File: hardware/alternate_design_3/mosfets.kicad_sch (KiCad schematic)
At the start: 3 parts, among them J2 Screw_Terminal_01x02, J3 Screw_Terminal_01x02, U5 ADUM3223ARZ

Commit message: updated alternate design
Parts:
- removed J2, J3: Screw_Terminal_01x02, symbol Connector:Screw_Terminal_01x02
- removed U5: ADUM3223ARZ, ADUM3223ARZ:SOIC127P600X175-16N, symbol ADUM3223ARZ:ADUM3223ARZ
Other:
- added sheet Gate Drive (gate_drive.kicad_sch)
- added sheet MCU (MCU.kicad_sch)
- added sheet OCP_Current_Sens (ocp_cur_sens.kicad_sch)
- added sheet Power Management (power_mgmt.kicad_sch)

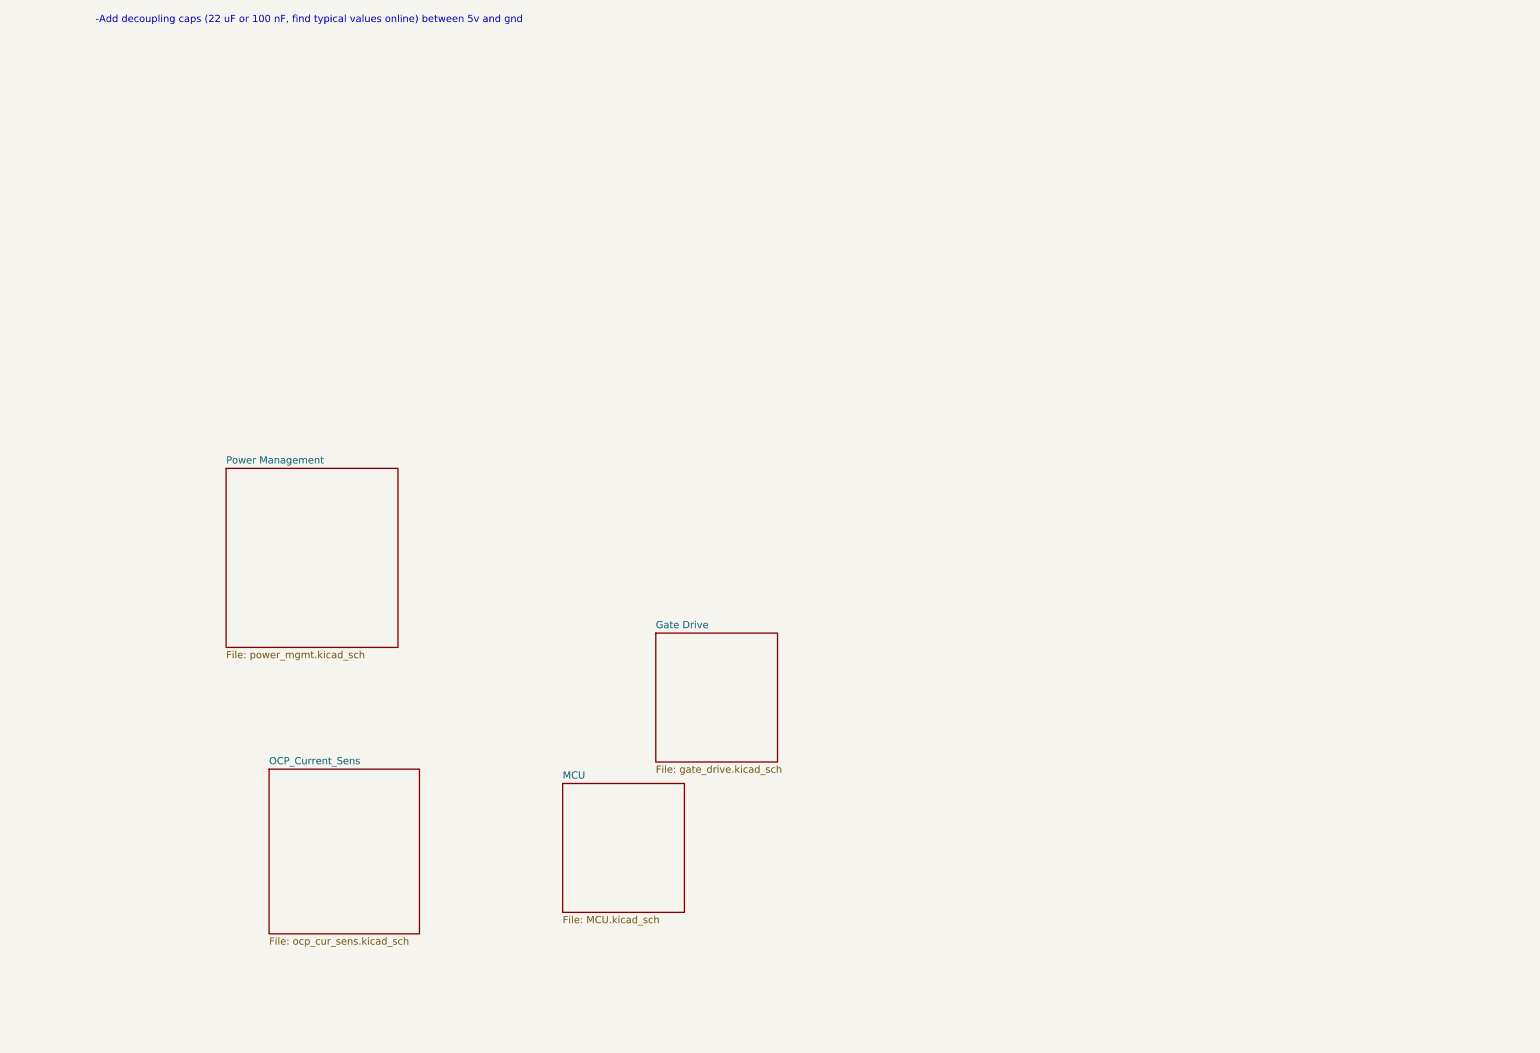
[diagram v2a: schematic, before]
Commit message: major additions to schematic of inverter
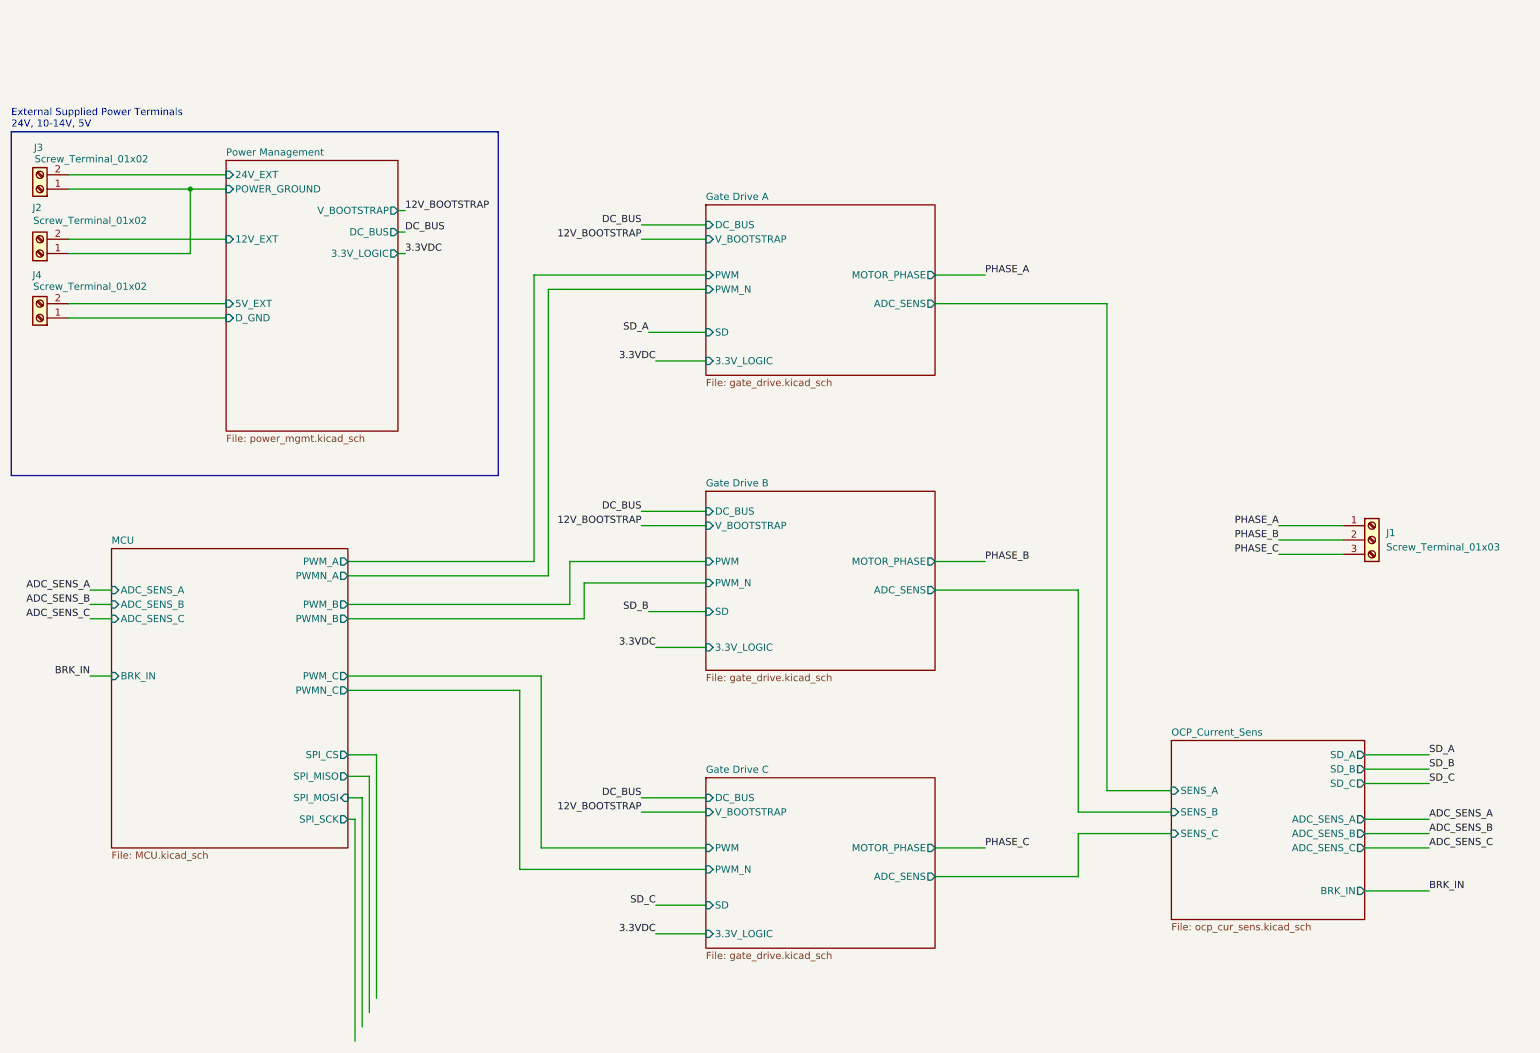
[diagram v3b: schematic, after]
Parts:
- added J1: Screw_Terminal_01x03, symbol Connector:Screw_Terminal_01x03
- added J2, J3, J4: Screw_Terminal_01x02, symbol Connector:Screw_Terminal_01x02
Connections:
- new net PHASE_A: J1.1 (Pin_1)
- new net PHASE_B: J1.2 (Pin_2)
- new net PHASE_C: J1.3 (Pin_3)
- new net Power Management/12V_EXT: J2.2 (Pin_2)
- new net Power Management/24V_EXT: J3.2 (Pin_2)
- new net Power Management/5V_EXT: J4.2 (Pin_2)
- new net Power Management/D_GND: J4.1 (Pin_1)
- new net Power Management/POWER_GROUND: J2.1 (Pin_1), J3.1 (Pin_1)
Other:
- sheet Gate Drive renamed Gate Drive A
- added sheet Gate Drive B (gate_drive.kicad_sch)
- added sheet Gate Drive C (gate_drive.kicad_sch)
- sheet Gate Drive A ports: added 3.3V_LOGIC, ADC_SENS, DC_BUS, MOTOR_PHASE, PWM, PWM_N, SD, V_BOOTSTRAP; removed none
- sheet MCU ports: added ADC_SENS_A, ADC_SENS_B, ADC_SENS_C, BRK_IN, PWMN_A, PWMN_B, PWMN_C, PWM_A, PWM_B, PWM_C, SPI_CS, SPI_MISO, SPI_MOSI, SPI_SCK; removed none
- sheet OCP_Current_Sens ports: added ADC_SENS_A, ADC_SENS_B, ADC_SENS_C, BRK_IN, SD_A, SD_B, SD_C, SENS_A, SENS_B, SENS_C; removed none
- sheet Power Management ports: added 12V_EXT, 24V_EXT, 3.3V_LOGIC, 5V_EXT, DC_BUS, D_GND, POWER_GROUND, V_BOOTSTRAP; removed none
- note added: "External Supplied Power Terminals 24V, 10-14V, 5V"
- note removed: "-Add decoupling caps (22 uF or 100 nF, find typical values online) between 5v and gnd"
- company: (none) -> Abdullah Abdullah and Fahad Al-Tamimi
- title: (none) -> Low Voltage BLDC motor inverter
